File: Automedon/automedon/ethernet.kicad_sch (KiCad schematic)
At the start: 4 parts, among them U10 DS108G-M2, U11 ER605v2, U18 OC200, U19 USB HUB

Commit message: Update bunch of other stuff - dont touch power
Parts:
- removed U19: USB HUB, symbol automedon:USB_PWR
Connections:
- net ANTENNA_ETH is gone; now on net GND: U10. (ETH_8)
- net ETH_DEBUG is gone; now on net GND: U10. (ETH_8)
- new net ETH_ANTENNA: U10. (ETH_8)
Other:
- note removed: "12V @ 3A"
- note removed: "PART LINK"
- moved on the sheet: U10, U11, U18

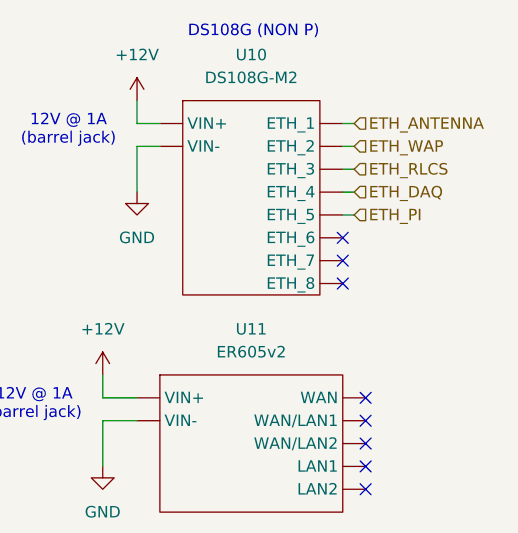
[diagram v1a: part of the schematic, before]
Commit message: Update eth ports
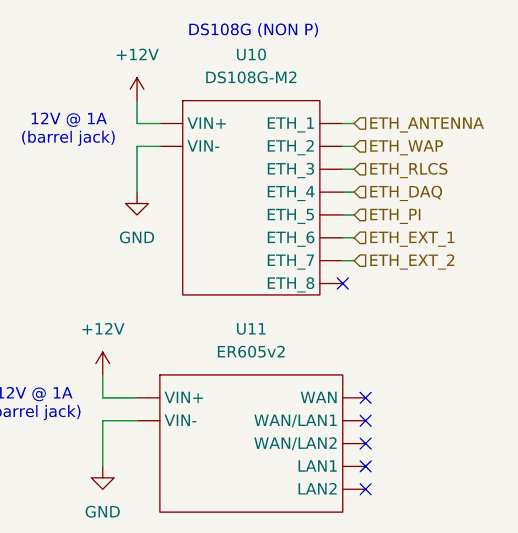
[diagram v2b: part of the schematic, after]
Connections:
- new net ETH_EXT_1: U10. (ETH_8)
- new net ETH_EXT_2: U10. (ETH_8)
- no-connect marks 10 -> 8
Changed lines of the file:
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@@
-	)
-	(no_connect
-		(at 162.56 85.09)
 	)
 	(no_connect
@@
 	(no_connect
 		(at 165.1 105.41)
-	)
-	(no_connect
-		(at 162.56 82.55)
 	)
 	(no_connect
@@
 		(pts
 			(xy 139.7 69.85) (xy 139.7 67.31)
+		)
+		(stroke
+			(width 0)
+			(type default)
+		)
+	)
+	(wire
+		(pts
+			(xy 162.56 82.55) (xy 163.83 82.55)
 		)
 		(stroke
@@
 	(wire
 		(pts
+			(xy 162.56 85.09) (xy 163.83 85.09)
+		)
+		(stroke
+			(width 0)
+			(type default)
+		)
+	)
+	(wire
+		(pts
 			(xy 163.83 72.39) (xy 162.56 72.39)
 		)
@@
 		)
 	)
+	(hierarchical_label "ETH_EXT_2"
+		(shape input)
+		(at 163.83 85.09 0)
+		(effects
+			(font
+				(size 1.27 1.27)
+			)
+			(justify left)
+		)
+	)
 	(hierarchical_label "ETH_RLCS"
 		(shape input)
@@
 		(effects
 			(font
+				(size 1.27 1.27)
+			)
+			(justify left)
+		)
+	)
+	(hierarchical_label "ETH_EXT_1"
+		(shape input)
+		(at 163.83 82.55 0)
+		(effects
+			(font

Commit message: Update connector
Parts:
- U10: value DS108G-M2 -> DS108G
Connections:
- net +12V: no longer U10. (ETH_8)
- new net: U11. (LAN2), U18. (ETH_2)
- new net: U10. (ETH_8), U11. (LAN2)
- new net +5V: U10. (ETH_8)
- no-connect marks 8 -> 4
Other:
- note added: "5V @ 0.5A (barrel jack)"
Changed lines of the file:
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@@
 	(generator_version "9.0")
 	(paper "A4")
-	(text "12V @ 1A \n(barrel jack)"
+	(text "5V @ 0.5A \n(barrel jack)"
 		(exclude_from_sim no)
 		(at 132.08 70.612 0)
@@
 	)
 	(no_connect
-		(at 162.56 128.27)
-	)
-	(no_connect
 		(at 165.1 107.95)
 	)
@@
 	)
 	(no_connect
-		(at 162.56 87.63)
-	)
-	(no_connect
 		(at 162.56 130.81)
 	)
-	(no_connect
-		(at 165.1 105.41)
-	)
-	(no_connect
-		(at 165.1 102.87)
-	)
 	(wire
 		(pts
@@
 	(wire
 		(pts
+			(xy 165.1 105.41) (xy 168.91 105.41)
+		)
+		(stroke
+			(width 0)
+			(type default)
+		)
+	)
+	(wire
+		(pts
+			(xy 168.91 105.41) (xy 168.91 128.27)
+		)
+		(stroke
+			(width 0)
+			(type default)
+		)
+	)
+	(wire
+		(pts
 			(xy 139.7 69.85) (xy 139.7 67.31)
 		)
@@
 	(wire
 		(pts
+			(xy 162.56 87.63) (xy 168.91 87.63)
+		)
+		(stroke
+			(width 0)
+			(type default)
+		)
+	)
+	(wire
+		(pts
 			(xy 139.7 72.39) (xy 142.24 72.39)
 		)
@@
 	(wire
 		(pts
+			(xy 168.91 87.63) (xy 168.91 102.87)
+		)
+		(stroke
+			(width 0)
+			(type default)
+		)
+	)
+	(wire
+		(pts
 			(xy 139.7 69.85) (xy 142.24 69.85)
+		)
+		(stroke
+			(width 0)
+			(type default)
+		)
+	)
+	(wire
+		(pts
+			(xy 168.91 128.27) (xy 162.56 128.27)
+		)
+		(stroke
+			(width 0)
+			(type default)
+		)
+	)
+	(wire
+		(pts
+			(xy 168.91 102.87) (xy 165.1 102.87)
 		)
 		(stroke
@@
 	)
 	(symbol
-		(lib_id "power:+12V")
+		(lib_id "automedon:ETH_SW")
+		(at 152.4 64.77 0)
+		(unit 1)
+		(exclude_from_sim no)
+		(in_bom yes)
+		(on_board yes)
+		(dnp no)
+		(fields_autoplaced yes)
+		(property "Reference" "U10"
+			(at 152.4 62.23 0)
+			(effects
+				(font
+					(size 1.27 1.27)
+				)
+			)
+		)
+		(property "Value" "DS108G"
+			(at 152.4 64.77 0)
+			(effects
+				(font
+					(size 1.27 1.27)
+				)
+			)
+		)
+		(property "Footprint" ""
+			(at 152.4 64.77 0)
+			(effects
+				(font
+					(size 1.27 1.27)
+				)
+				(hide yes)
+			)
+		)
+		(property "Datasheet" ""
+			(at 152.4 64.77 0)
+			(effects
+				(font
+					(size 1.27 1.27)
+				)
+				(hide yes)
+			)
+		)
+		(property "Description" ""
+			(at 152.4 64.77 0)
+			(effects
+				(font
+					(size 1.27 1.27)
+				)
+				(hide yes)
+			)
+		)
+		(pin ""
+		)
+		(pin ""
+		)
+		(pin ""
+		)
+		(pin ""
+		)
+		(pin ""
+		)
+		(pin ""
+		)
+		(pin ""
+		)
+		(pin ""
+		)
+		(pin ""
+		)
+		(pin ""
+		)
+		(instances
+			(project ""
+				(path "/75831ec5-d9f4-4d6d-a97b-0bb87f785768/a01756e2-dff9-4d90-8b5d-2eadc2973bae"
+					(reference "U10")
+					(unit 1)
+				)
+			)
+		)
+	)
+	(symbol
+		(lib_id "power:GND")
+		(at 139.7 77.47 0)
+		(unit 1)
+		(exclude_from_sim no)
+		(in_bom yes)
+		(on_board yes)
+		(dnp no)
+		(fields_autoplaced yes)
+		(property "Reference" "#PWR020"
+			(at 139.7 83.82 0)
+			(effects
+				(font
+					(size 1.27 1.27)
+				)
+				(hide yes)
+			)
+		)
+		(property "Value" "GND"
+			(at 139.7 82.55 0)
+			(effects
+				(font
+					(size 1.27 1.27)
+				)
+			)
+		)
+		(property "Footprint" ""
+			(at 139.7 77.47 0)
+			(effects
+				(font
+					(size 1.27 1.27)
+				)
+				(hide yes)
+			)
+		)
+		(property "Datasheet" ""
+			(at 139.7 77.47 0)
+			(effects
+				(font
+					(size 1.27 1.27)
+				)
+				(hide yes)
+			)
+		)
+		(property "Description" "Power symbol creates a global label with name \"GND\" , ground"
+			(at 139.7 77.47 0)
+			(effects
+				(font
+					(size 1.27 1.27)
+				)
+				(hide yes)
+			)
+		)
+		(pin "1"
+		)
+		(instances
+			(project ""
+				(path "/75831ec5-d9f4-4d6d-a97b-0bb87f785768/a01756e2-dff9-4d90-8b5d-2eadc2973bae"
+					(reference "#PWR020")
+					(unit 1)
+				)
+			)
+		)
+	)
+	(symbol
+		(lib_id "power:+5V")
 		(at 139.7 67.31 0)
 		(unit 1)
@@
 			)
 		)
-		(property "Value" "+12V"
+		(property "Value" "+5V"
 			(at 139.7 62.23 0)
 			(effects
@@
 			)
 		)
-		(property "Description" "Power symbol creates a global label with name \"+12V\""
+		(property "Description" "Power symbol creates a global label with name \"+5V\""
 			(at 139.7 67.31 0)
 			(effects
@@
 					(unit 1)
 				)
-			)
-		)
-	)
-	(symbol
-		(lib_id "automedon:ETH_SW")
-		(at 152.4 64.77 0)
-		(unit 1)
-		(exclude_from_sim no)
-		(in_bom yes)
-		(on_board yes)
-		(dnp no)
-		(fields_autoplaced yes)
-		(property "Reference" "U10"
-			(at 152.4 62.23 0)
-			(effects
-				(font
-					(size 1.27 1.27)
-				)
-			)
-		)
-		(property "Value" "DS108G-M2"
-			(at 152.4 64.77 0)
-			(effects
-				(font
-					(size 1.27 1.27)
-				)
-			)
-		)
-		(property "Footprint" ""
-			(at 152.4 64.77 0)
-			(effects
-				(font
-					(size 1.27 1.27)
-				)
-				(hide yes)
-			)
-		)
-		(property "Datasheet" ""
-			(at 152.4 64.77 0)
-			(effects
-				(font
-					(size 1.27 1.27)
-				)
-				(hide yes)
-			)
-		)
-		(property "Description" ""
-			(at 152.4 64.77 0)
-			(effects
-				(font
-					(size 1.27 1.27)
-				)
-				(hide yes)
-			)
-		)
-		(pin ""
-		)
-		(pin ""
-		)
-		(pin ""
-		)
-		(pin ""
-		)
-		(pin ""
-		)
-		(pin ""
-		)
-		(pin ""
-		)
-		(pin ""
-		)
-		(pin ""
-		)
-		(pin ""
-		)
-		(instances
-			(project ""
-				(path "/75831ec5-d9f4-4d6d-a97b-0bb87f785768/a01756e2-dff9-4d90-8b5d-2eadc2973bae"
-					(reference "U10")
-					(unit 1)
-				)
-			)
-		)
-	)
-	(symbol
-		(lib_id "power:GND")
-		(at 139.7 77.47 0)
-		(unit 1)
-		(exclude_from_sim no)
-		(in_bom yes)
-		(on_board yes)
-		(dnp no)
-		(fields_autoplaced yes)
-		(property "Reference" "#PWR020"
-			(at 139.7 83.82 0)
-			(effects
-				(font
-					(size 1.27 1.27)
-				)
-				(hide yes)
-			)
-		)
-		(property "Value" "GND"
-			(at 139.7 82.55 0)
-			(effects
-				(font
-					(size 1.27 1.27)
-				)
-			)
-		)
-		(property "Footprint" ""
-			(at 139.7 77.47 0)
-			(effects
-				(font
-					(size 1.27 1.27)
-				)
-				(hide yes)
-			)
-		)
-		(property "Datasheet" ""
-			(at 139.7 77.47 0)
-			(effects
-				(font
-					(size 1.27 1.27)
-				)
-				(hide yes)
-			)
-		)
-		(property "Description" "Power symbol creates a global label with name \"GND\" , ground"
-			(at 139.7 77.47 0)
-			(effects
-				(font
-					(size 1.27 1.27)
-				)
-				(hide yes)
-			)
-		)
-		(pin "1"
-		)
-		(instances
-			(project ""
-				(path "/75831ec5-d9f4-4d6d-a97b-0bb87f785768/a01756e2-dff9-4d90-8b5d-2eadc2973bae"
-					(reference "#PWR020")
-					(unit 1)
-				)

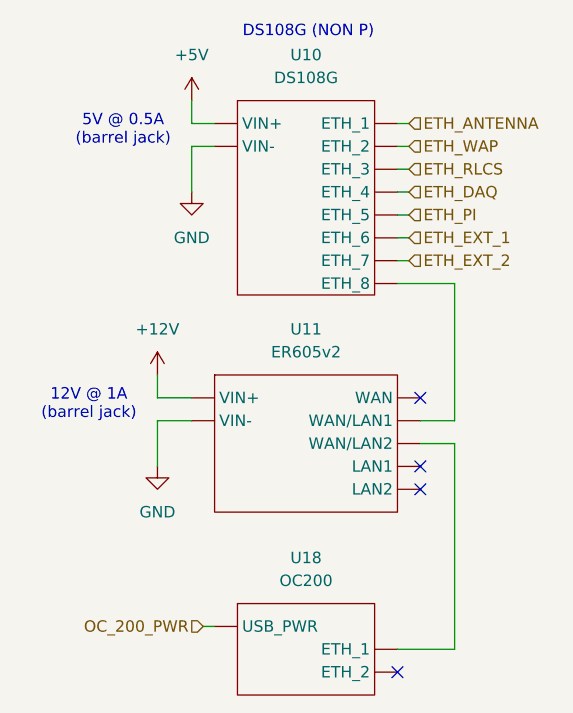
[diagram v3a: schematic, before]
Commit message: Revert "Update connector"
This reverts commit 3a37b6a19b99deb2b7118eab30d8044c58bd28a2.
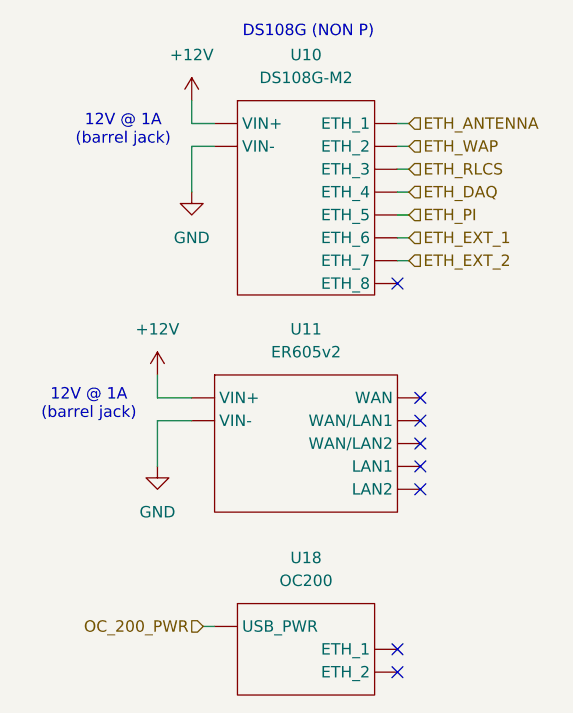
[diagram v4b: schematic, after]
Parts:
- U10: value DS108G -> DS108G-M2
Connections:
- net +5V is gone; now on net GND: U10. (ETH_8)
- net +12V: now also U10. (ETH_8)
- no-connect marks 4 -> 8
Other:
- note removed: "5V @ 0.5A (barrel jack)"
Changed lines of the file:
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@@
 	(generator_version "9.0")
 	(paper "A4")
-	(text "5V @ 0.5A \n(barrel jack)"
+	(text "12V @ 1A \n(barrel jack)"
 		(exclude_from_sim no)
 		(at 132.08 70.612 0)
@@
 	)
 	(no_connect
+		(at 162.56 128.27)
+	)
+	(no_connect
 		(at 165.1 107.95)
 	)
@@
 	)
 	(no_connect
+		(at 162.56 87.63)
+	)
+	(no_connect
 		(at 162.56 130.81)
 	)
+	(no_connect
+		(at 165.1 105.41)
+	)
+	(no_connect
+		(at 165.1 102.87)
+	)
 	(wire
 		(pts
@@
 	(wire
 		(pts
-			(xy 165.1 105.41) (xy 168.91 105.41)
-		)
-		(stroke
-			(width 0)
-			(type default)
-		)
-	)
-	(wire
-		(pts
-			(xy 168.91 105.41) (xy 168.91 128.27)
-		)
-		(stroke
-			(width 0)
-			(type default)
-		)
-	)
-	(wire
-		(pts
 			(xy 139.7 69.85) (xy 139.7 67.31)
 		)
@@
 	(wire
 		(pts
-			(xy 162.56 87.63) (xy 168.91 87.63)
-		)
-		(stroke
-			(width 0)
-			(type default)
-		)
-	)
-	(wire
-		(pts
 			(xy 139.7 72.39) (xy 142.24 72.39)
 		)
@@
 	(wire
 		(pts
-			(xy 168.91 87.63) (xy 168.91 102.87)
-		)
-		(stroke
-			(width 0)
-			(type default)
-		)
-	)
-	(wire
-		(pts
 			(xy 139.7 69.85) (xy 142.24 69.85)
-		)
-		(stroke
-			(width 0)
-			(type default)
-		)
-	)
-	(wire
-		(pts
-			(xy 168.91 128.27) (xy 162.56 128.27)
-		)
-		(stroke
-			(width 0)
-			(type default)
-		)
-	)
-	(wire
-		(pts
-			(xy 168.91 102.87) (xy 165.1 102.87)
 		)
 		(stroke
@@
 	)
 	(symbol
+		(lib_id "power:+12V")
+		(at 139.7 67.31 0)
+		(unit 1)
+		(exclude_from_sim no)
+		(in_bom yes)
+		(on_board yes)
+		(dnp no)
+		(fields_autoplaced yes)
+		(property "Reference" "#PWR019"
+			(at 139.7 71.12 0)
+			(effects
+				(font
+					(size 1.27 1.27)
+				)
+				(hide yes)
+			)
+		)
+		(property "Value" "+12V"
+			(at 139.7 62.23 0)
+			(effects
+				(font
+					(size 1.27 1.27)
+				)
+			)
+		)
+		(property "Footprint" ""
+			(at 139.7 67.31 0)
+			(effects
+				(font
+					(size 1.27 1.27)
+				)
+				(hide yes)
+			)
+		)
+		(property "Datasheet" ""
+			(at 139.7 67.31 0)
+			(effects
+				(font
+					(size 1.27 1.27)
+				)
+				(hide yes)
+			)
+		)
+		(property "Description" "Power symbol creates a global label with name \"+12V\""
+			(at 139.7 67.31 0)
+			(effects
+				(font
+					(size 1.27 1.27)
+				)
+				(hide yes)
+			)
+		)
+		(pin "1"
+		)
+		(instances
+			(project ""
+				(path "/75831ec5-d9f4-4d6d-a97b-0bb87f785768/a01756e2-dff9-4d90-8b5d-2eadc2973bae"
+					(reference "#PWR019")
+					(unit 1)
+				)
+			)
+		)
+	)
+	(symbol
 		(lib_id "automedon:ETH_SW")
 		(at 152.4 64.77 0)
@@
 			)
 		)
-		(property "Value" "DS108G"
+		(property "Value" "DS108G-M2"
 			(at 152.4 64.77 0)
 			(effects
@@
 					(unit 1)
 				)
-			)
-		)
-	)
-	(symbol
-		(lib_id "power:+5V")
-		(at 139.7 67.31 0)
-		(unit 1)
-		(exclude_from_sim no)
-		(in_bom yes)
-		(on_board yes)
-		(dnp no)
-		(fields_autoplaced yes)
-		(property "Reference" "#PWR019"
-			(at 139.7 71.12 0)
-			(effects
-				(font
-					(size 1.27 1.27)
-				)
-				(hide yes)
-			)
-		)
-		(property "Value" "+5V"
-			(at 139.7 62.23 0)
-			(effects
-				(font
-					(size 1.27 1.27)
-				)
-			)
-		)
-		(property "Footprint" ""
-			(at 139.7 67.31 0)
-			(effects
-				(font
-					(size 1.27 1.27)
-				)
-				(hide yes)
-			)
-		)
-		(property "Datasheet" ""
-			(at 139.7 67.31 0)
-			(effects
-				(font
-					(size 1.27 1.27)
-				)
-				(hide yes)
-			)
-		)
-		(property "Description" "Power symbol creates a global label with name \"+5V\""
-			(at 139.7 67.31 0)
-			(effects
-				(font
-					(size 1.27 1.27)
-				)
-				(hide yes)
-			)
-		)
-		(pin "1"
-		)
-		(instances
-			(project ""
-				(path "/75831ec5-d9f4-4d6d-a97b-0bb87f785768/a01756e2-dff9-4d90-8b5d-2eadc2973bae"
-					(reference "#PWR019")
-					(unit 1)
-				)
